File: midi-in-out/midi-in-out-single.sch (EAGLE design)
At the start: 38 parts, among them X1 2510-, X2 MAB5SH, X3 MAB5SH, X4 MAB5SH, X5 MAB5SH, X6 2510-

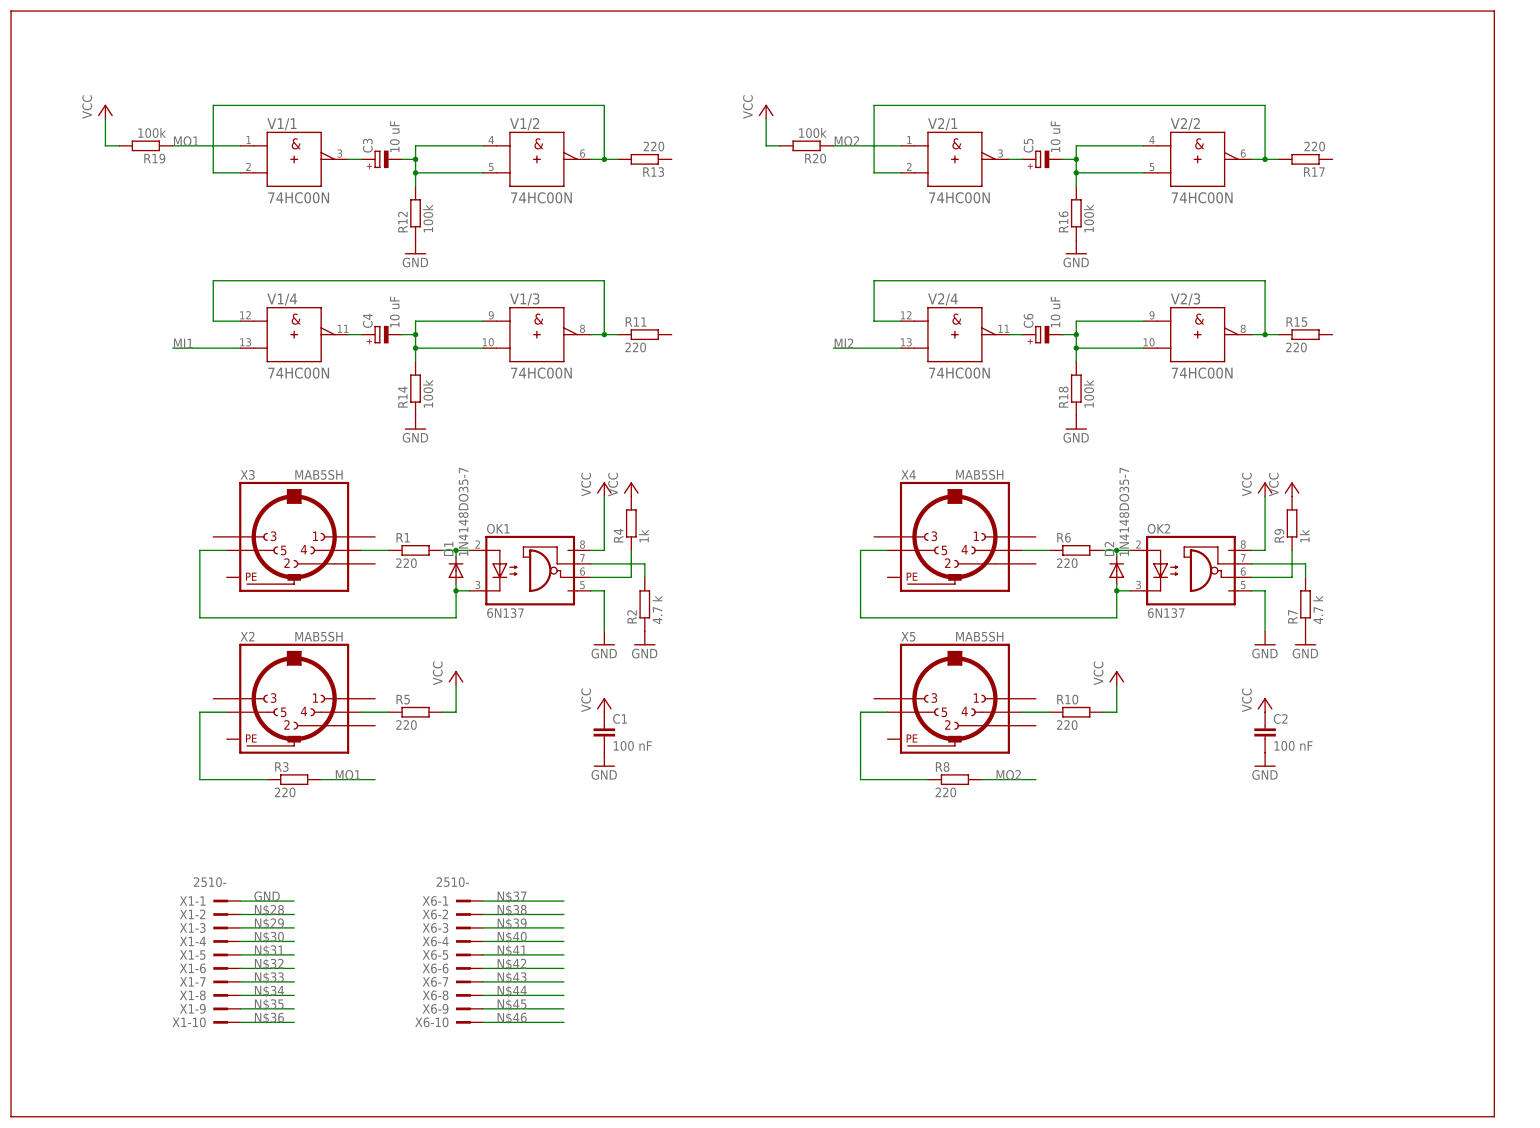
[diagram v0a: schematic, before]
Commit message: midi-in-out edits
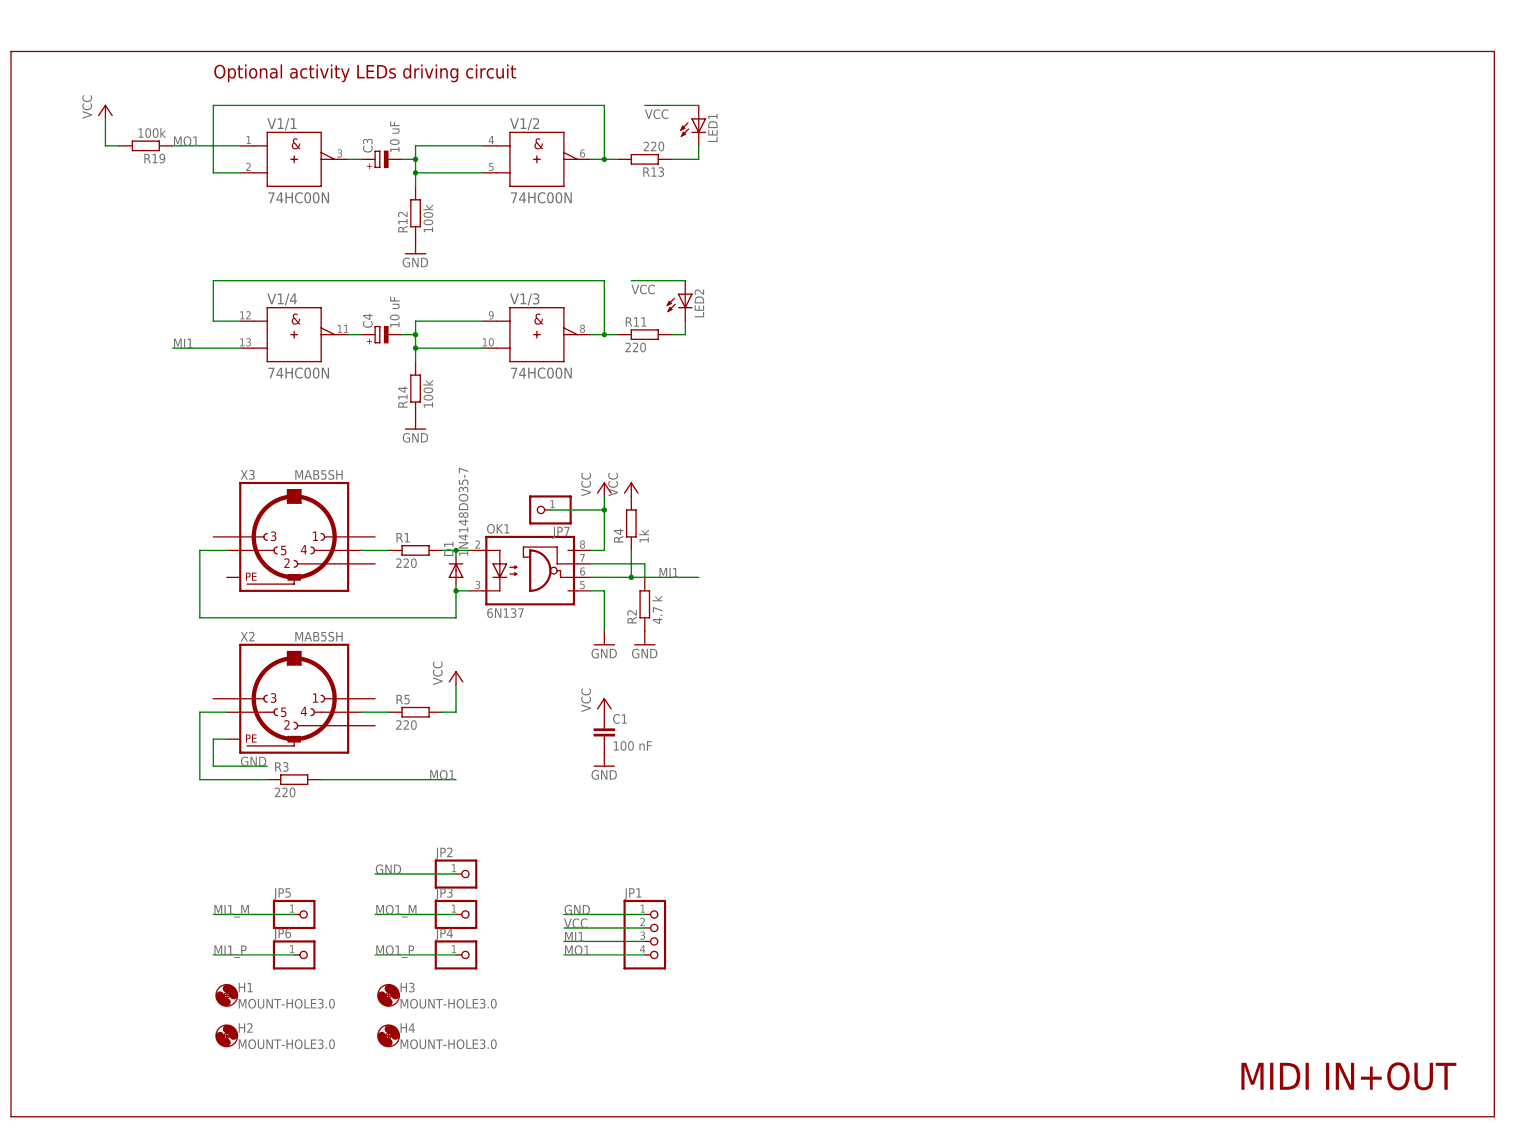
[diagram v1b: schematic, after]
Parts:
- removed C2: 100 nF, rcl:C-EU025-024X044
- removed C5, C6: 10 uF, rcl:CPOL-EUE2.5-5
- removed D2: 1N4148DO35-7, diode:1N4148DO35-7
- removed OK2: 6N137, optocoupler:6N137
- removed R10, R15, R17, R6, R8: 220, rcl:R-EU_0204/7
- removed R16, R18, R20: 100k, rcl:R-EU_0204/7
- removed R7: 4.7 k, rcl:R-EU_0204/7
- removed R9: 1k, rcl:R-EU_0204/7
- removed V2: 74HC00N, 74ttl-din:74HC00N
- removed X1, X6: 2510-, con-3m:2510-
- removed X4, X5: MAB5SH, con-hirschmann:MAB5SH
- added H1, H2, H3, H4: MOUNT-HOLE3.0, holes:MOUNT-HOLE3.0
- added JP1: (no value), pinhead:PINHD-1X4/90
- added JP2, JP3, JP4, JP5, JP6, JP7: (no value), pinhead:PINHD-1X1
- added LED1, LED2: (no value), led:LED3MM
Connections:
- removed net MI2: V2/4.B
- removed net MO2: R20.1, R8.2, V2/1.A
- removed net N$11: R6.1, X4.4
- removed net N$12: R8.1, X5.5
- removed net N$13: OK2.VO, R9.1
- removed net N$14: R10.1, X5.4
- removed net N$2: D1.A, OK1.C, X3.5
- removed net N$21: C5.-, R16.2, V2/2.A, V2/2.B
- removed net N$22: C5.+, V2/1.Y
- removed net N$23: R17.2, V2/1.B, V2/2.Y
- removed net N$24: C6.+, V2/4.Y
- removed net N$25: C6.-, R18.2, V2/3.A, V2/3.B
- removed net N$26: R15.1, V2/3.Y, V2/4.A
- removed net N$28: X1-2.KL
- removed net N$29: X1-3.KL
- removed net N$30: X1-4.KL
- removed net N$31: X1-5.KL
- removed net N$32: X1-6.KL
- removed net N$33: X1-7.KL
- removed net N$34: X1-8.KL
- removed net N$35: X1-9.KL
- removed net N$36: X1-10.KL
- removed net N$37: X6-1.KL
- removed net N$38: X6-2.KL
- removed net N$39: X6-3.KL
- removed net N$4: R1.1, X3.4
- removed net N$40: X6-4.KL
- removed net N$41: X6-5.KL
- removed net N$42: X6-6.KL
- removed net N$43: X6-7.KL
- removed net N$44: X6-8.KL
- removed net N$45: X6-9.KL
- removed net N$46: X6-10.KL
- removed net N$5: OK1.VO, R4.1
- removed net N$6: R3.1, X2.5
- removed net N$7: R5.1, X2.4
- removed net N$9: D2.A, OK2.C, X4.5
- new net MI1_M: D1.A, JP5.1, OK1.C, X3.5
- new net MI1_P: JP6.1, R1.1, X3.4
- new net MO1_M: JP3.1, R3.1, X2.5
- new net MO1_P: JP4.1, R5.1, X2.4
- net GND: now also JP1.1, JP2.1, X2.PE; no longer C2.2, OK2.GND, R16.1, R18.1, R7.1, X1-1.KL
- net MI1: now also JP1.3, OK1.VO, R4.1
- net MO1: now also JP1.4
- net N$10: now also LED1.C, R13.1; no longer OK2.VE, R7.2
- net N$8: now also LED2.C, R11.2; no longer D2.C, OK2.A, R6.2
- net VCC: now also JP1.2, JP7.1, LED1.A, LED2.A; no longer C2.1, OK2.VCC, R10.2, R20.2, R9.2
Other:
- note added: "MIDI IN+OUT"
- note added: "Optional activity LEDs driving circuit"
